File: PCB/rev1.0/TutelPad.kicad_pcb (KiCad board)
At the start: 2 copper layers, 120 x 42 mm, 16 parts, among them SW1 SW_Push, U1 generic-promicro

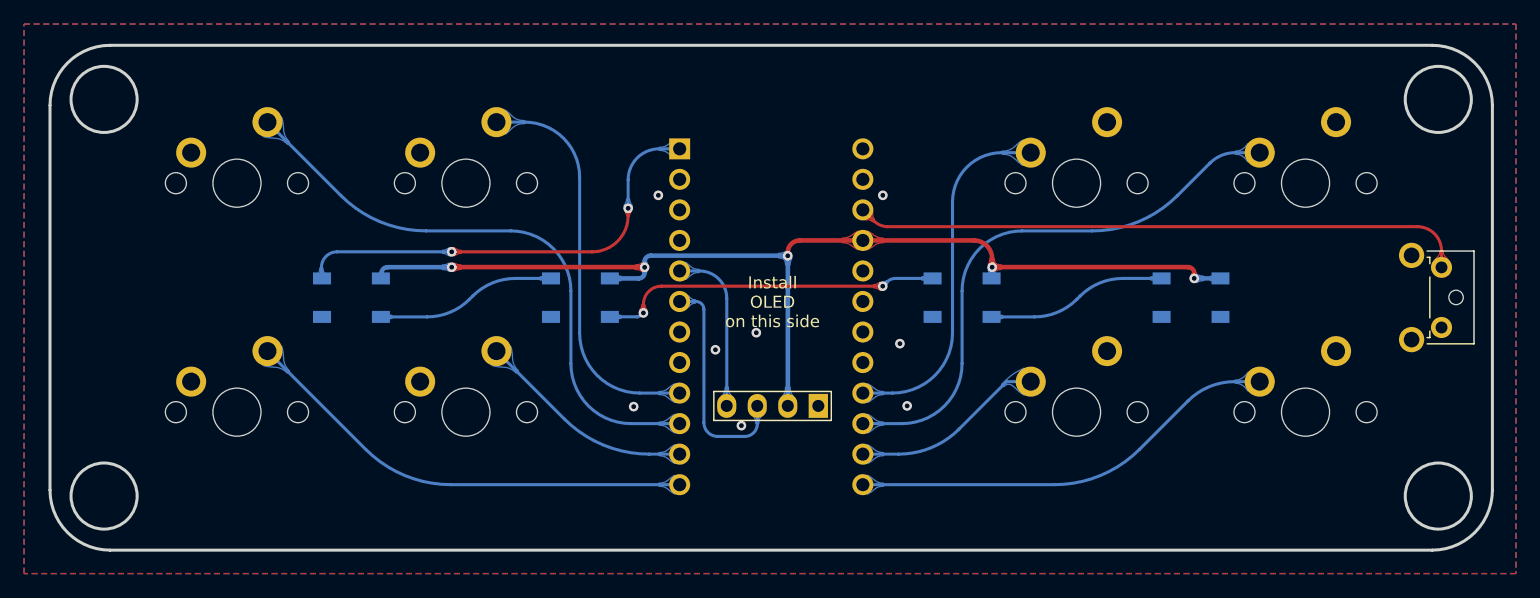
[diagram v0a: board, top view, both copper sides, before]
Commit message: fixing the readme
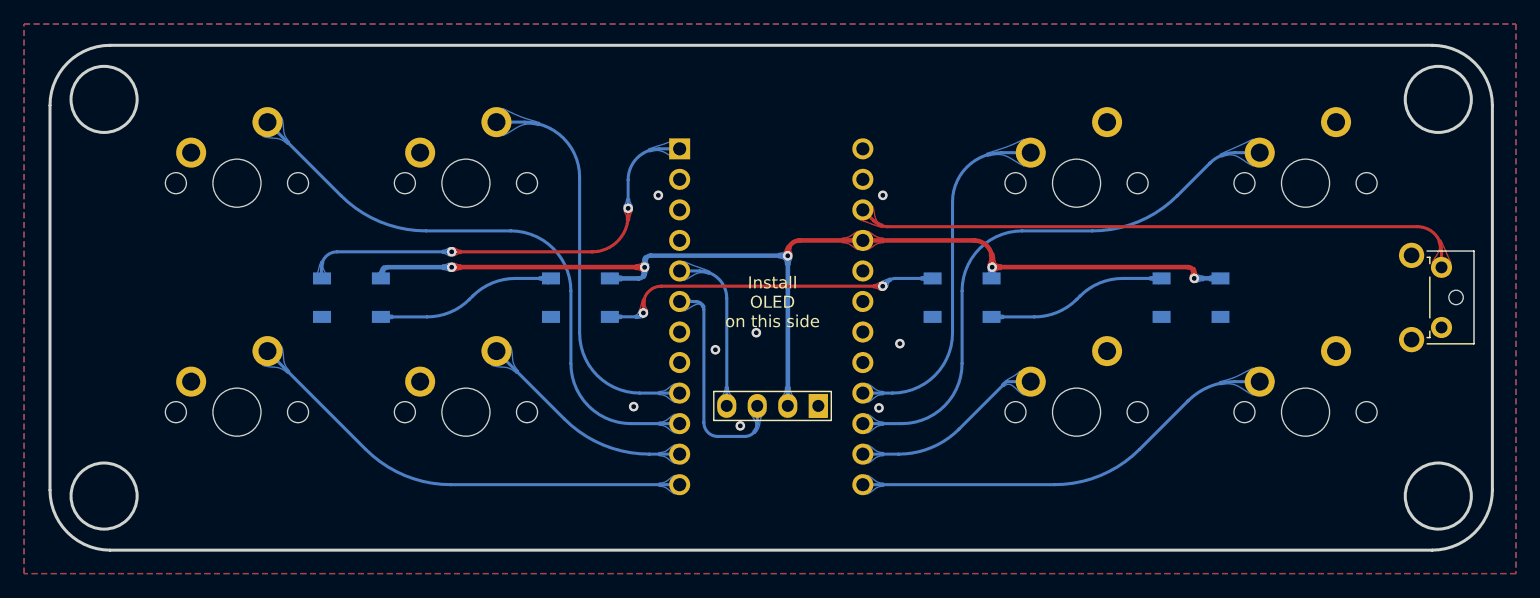
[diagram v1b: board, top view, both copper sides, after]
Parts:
- added G***: 0xCB, 0xcb:0xCB, B.Cu at (167.6, 110.9)

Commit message: OSHW
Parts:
- added REF**: OSHW-Logo2_7.3x6mm_SilkScreen, Symbol:OSHW-Logo2_7.3x6mm_SilkScreen, B.Cu at (153.7, 114.2)
